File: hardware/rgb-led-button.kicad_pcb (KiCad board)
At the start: 2 copper layers, 25 x 25 mm, 25 parts, among them P1 CON-SENSOR, P2 Boot, SW1 RGB_SWITCH_AD, U1 XMC1100-16, U2 DRILL, U3 DRILL, U4 DRILL, U5 DRILL

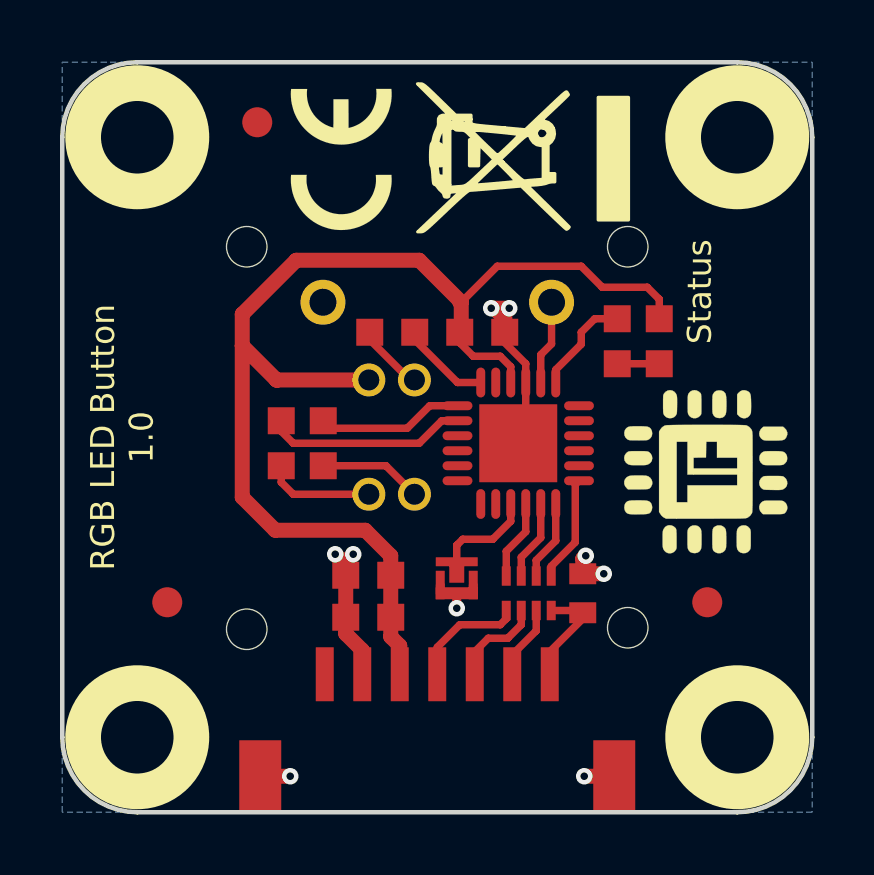
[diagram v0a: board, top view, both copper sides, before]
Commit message: Change capacitor footprint(s) to C0402F
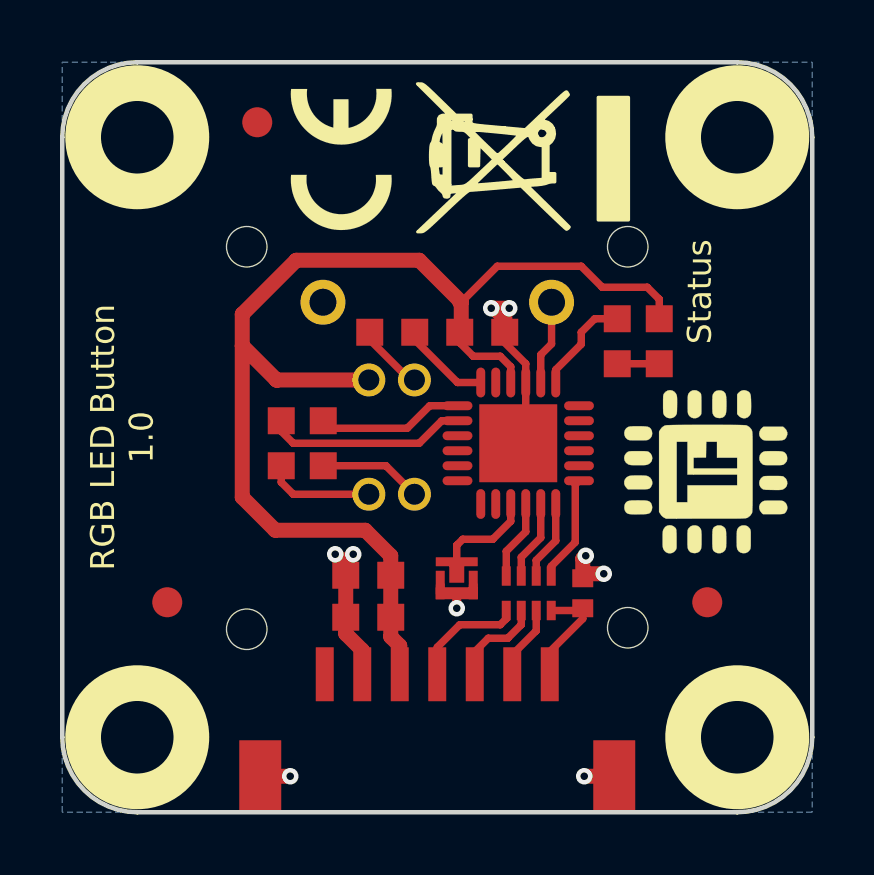
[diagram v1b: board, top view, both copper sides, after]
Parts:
- C1: footprint C0402E -> kicad-libraries:C0402F
- R2, R3, R4: footprint R0603F -> kicad-libraries:R0603F
- RP1: footprint 4X0402 -> kicad-libraries:4X0402
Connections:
- P1 pad 1: (no net) -> Net-(P1-Pad1)
- U1 pad 11: (no net) -> Net-(U1-Pad11)
- U1 pad 15: (no net) -> Net-(U1-Pad15)
- U1 pad 16: (no net) -> Net-(U1-Pad16)
- U1 pad 17: (no net) -> Net-(U1-Pad17)
- U1 pad 18: (no net) -> Net-(U1-Pad18)
- U1 pad 19: (no net) -> Net-(U1-Pad19)
- U1 pad 2: (no net) -> Net-(U1-Pad2)
- U1 pad 20: (no net) -> Net-(U1-Pad20)
- U1 pad 3: (no net) -> Net-(U1-Pad3)
- U1 pad 4: (no net) -> Net-(U1-Pad4)
- U1 pad 5: (no net) -> Net-(U1-Pad5)
- U1 pad 6: (no net) -> Net-(U1-Pad6)
